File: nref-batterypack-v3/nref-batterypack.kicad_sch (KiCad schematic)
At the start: 90 parts, among them J0 C1-, J1 C1-, J2 C2+, J3 C3-, J4 C4+, J5 PACK_CONN, J6 BACK_CONN, Q1 BC817, Q2 BC817, Q3 BC817, Q4 BC817, Q5 AO3401A, Q7 AO3401A, Q8 Q_Dual_NMOS_Picostar_CSD87501L, U1 BQ76922

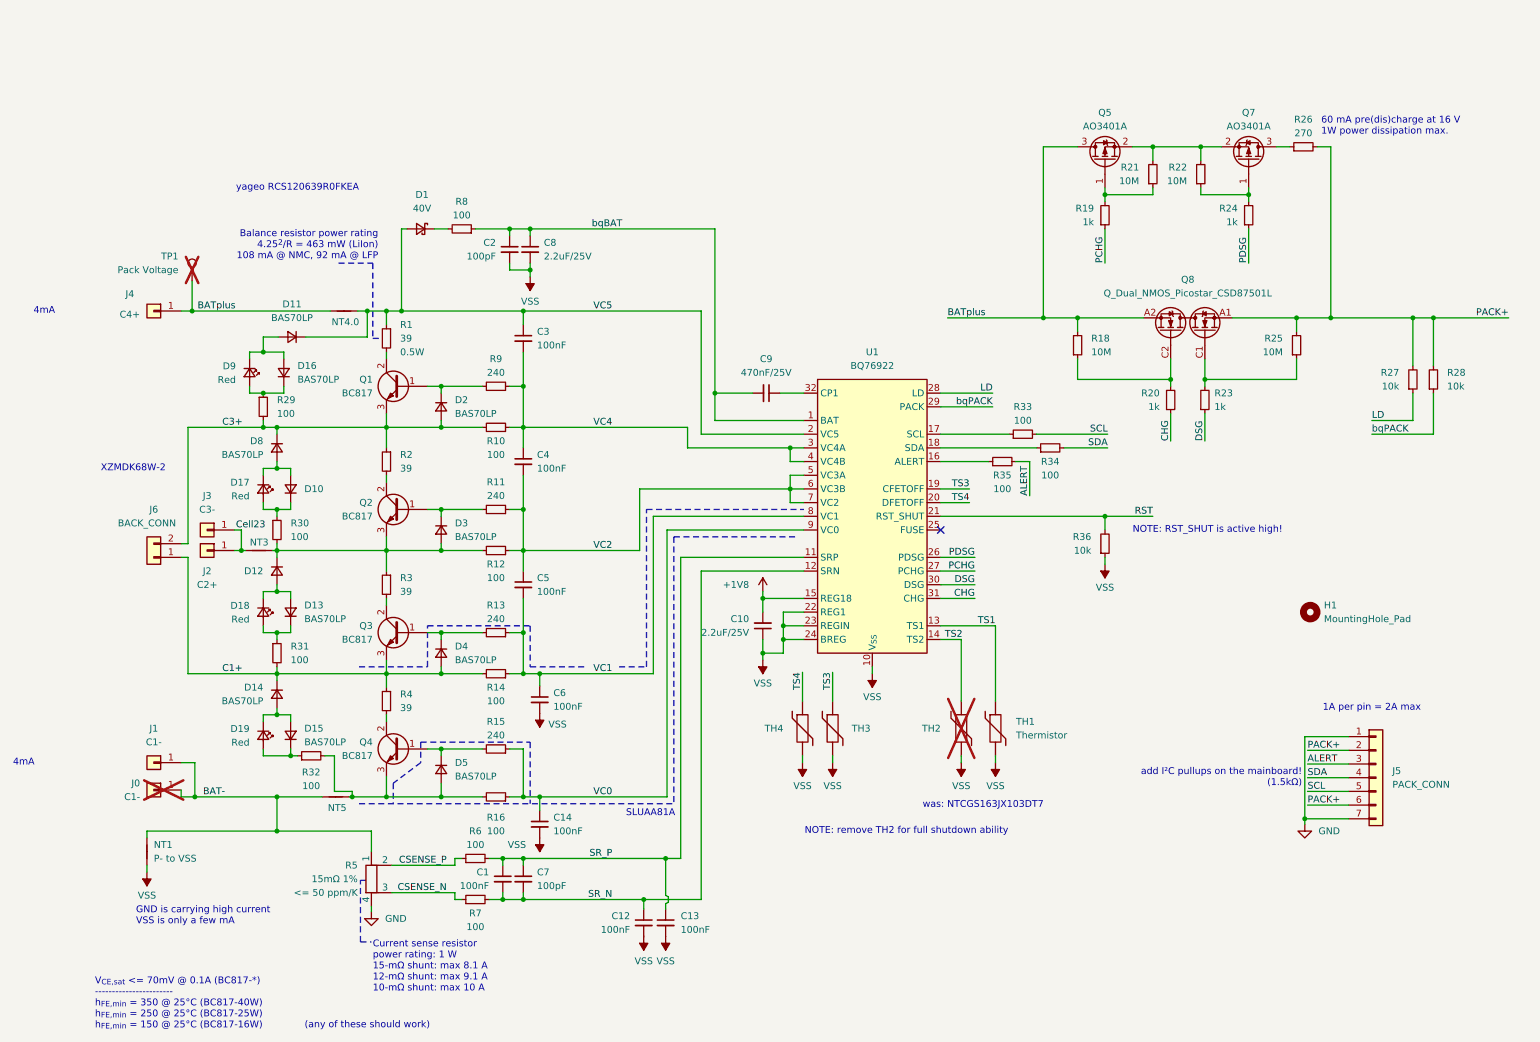
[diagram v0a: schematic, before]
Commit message: small schematic cleanups for book
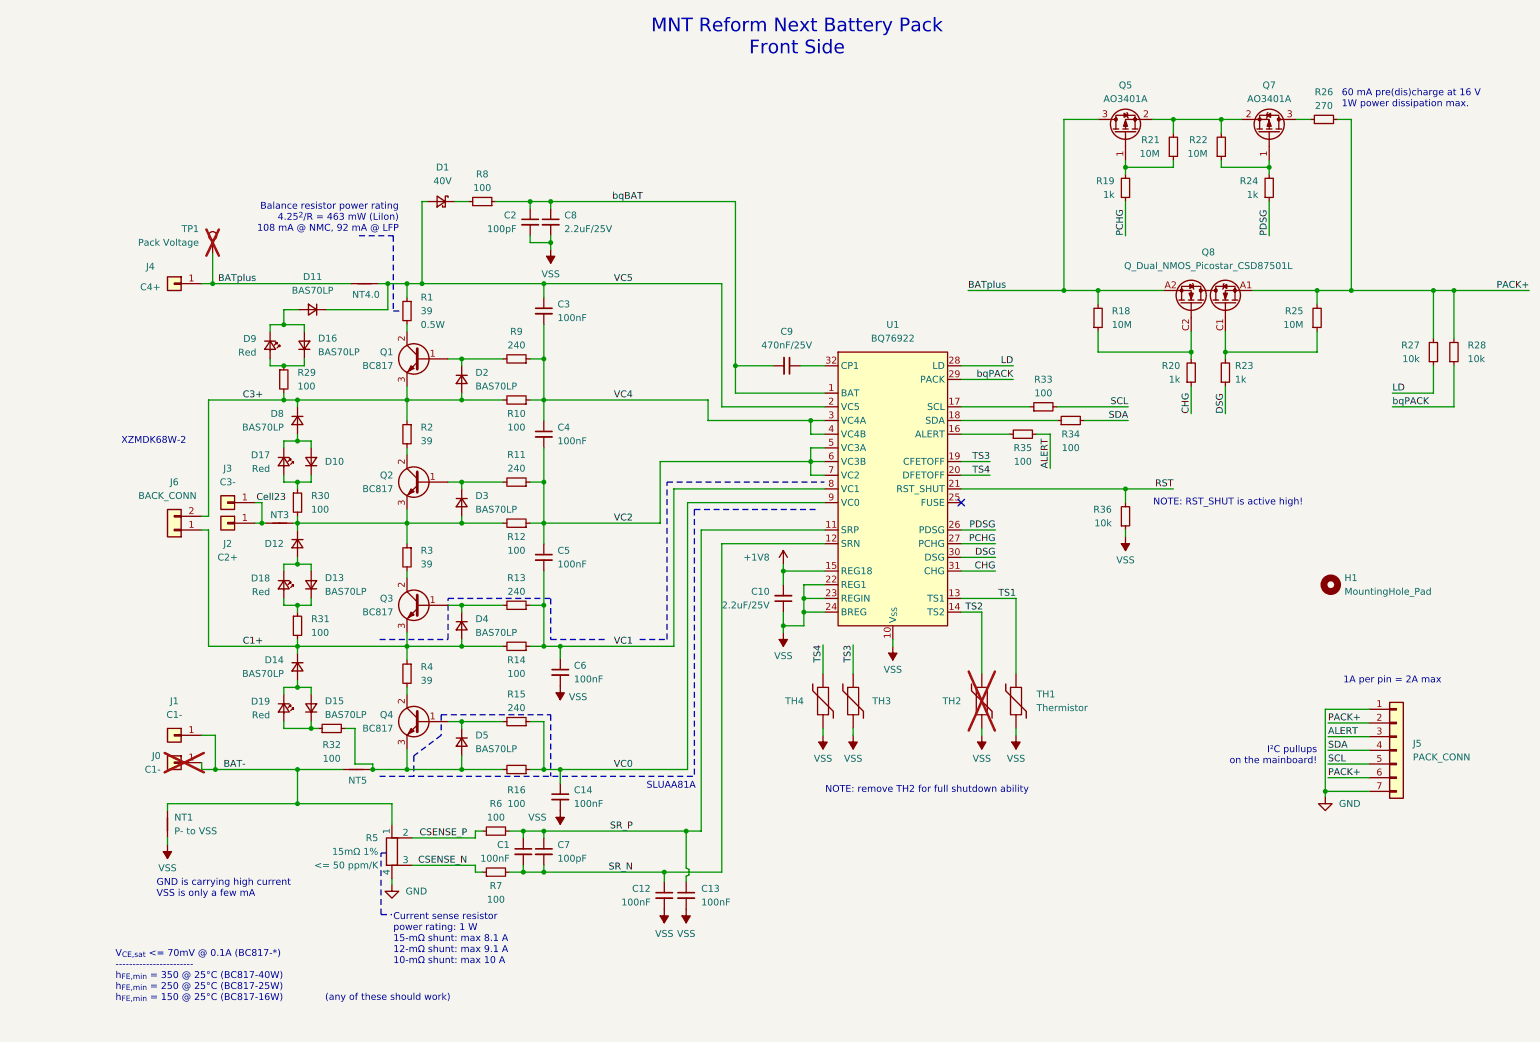
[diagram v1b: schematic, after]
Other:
- note added: "I²C pullups on the mainboard!"
- note added: "MNT Reform Next Battery Pack Front Side"
- note removed: "4mA"
- note removed: "add I²C pullups on the mainboard! (1.5kΩ)"
- note removed: "was: NTCGS163JX103DT7"
- note removed: "yageo RCS120639R0FKEA"
- company: (none) -> MNT Research GmbH, Copyright 2026
- title: (none) -> MNT Reform Next Battery Pack (Front)
- moved on the sheet: C1, C10, C12, C13, C14, C2, C3, C4, C5, C6, C7, C8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
